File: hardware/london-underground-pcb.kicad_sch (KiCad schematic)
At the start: 335 parts

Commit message: first 150 LEDS placed
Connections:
- net LED10 is gone; now on net ROW10: LED91.4 (DI)
- net LED11 is gone; now on net ROW11: LED101.4 (DI)
- net LED12 is gone; now on net ROW12: LED111.4 (DI)
- net LED13 is gone; now on net ROW13: LED121.4 (DI)
- net LED14 is gone; now on net ROW14: LED131.4 (DI)
- net LED15 is gone; now on net ROW15: LED141.4 (DI)
- net LED16 is gone; now on net ROW16: LED151.4 (DI)
- net LED17 is gone; now on net ROW17: LED161.4 (DI)
- net LED18 is gone; now on net ROW18: LED171.4 (DI)
- net LED19 is gone; now on net ROW19: LED181.4 (DI)
- net LED2 is gone; now on net ROW2: LED11.4 (DI)
- net LED20 is gone; now on net ROW20: LED191.4 (DI)
- net LED21 is gone; now on net ROW21: LED201.4 (DI)
- net LED22 is gone; now on net ROW22: LED211.4 (DI)
- net LED23 is gone; now on net ROW23: LED221.4 (DI)
- net LED24 is gone; now on net ROW24: LED231.4 (DI)
- net LED25 is gone; now on net ROW25: LED241.4 (DI)
- net LED26 is gone; now on net ROW26: LED251.4 (DI)
- net LED27 is gone; now on net ROW27: LED261.4 (DI)
- net LED28 is gone; now on net ROW28: LED271.4 (DI)
- net LED29 is gone; now on net ROW29: LED281.4 (DI)
- net LED3 is gone; now on net ROW3: LED21.4 (DI)
- net LED30 is gone; now on net ROW30: LED291.4 (DI)
- net LED4 is gone; now on net ROW4: LED31.4 (DI)
- net LED5 is gone; now on net ROW5: LED41.4 (DI)
- net LED6 is gone; now on net ROW6: LED51.4 (DI)
- net LED7 is gone; now on net ROW7: LED61.4 (DI)
- net LED8 is gone; now on net ROW8: LED71.4 (DI)
- net LED9 is gone; now on net ROW9: LED81.4 (DI)

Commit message: Placed 570 LEDS,
Still need to do the routing
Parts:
- added LED301, LED302, LED303, LED304, LED305, LED306, LED307, LED308, LED309, LED310, LED311, LED312, LED313, LED314, LED315, LED316, LED317, LED318, LED319, LED320, LED321, LED322, LED323, LED324, LED325, LED326, LED327, LED328, LED329, LED330, LED331, LED332, LED333, LED334, LED335, LED336, LED337, LED338, LED339, LED340, LED341, LED342, LED343, LED344, LED345, LED346, LED347, LED348, LED349, LED350, LED351, LED352, LED353, LED354, LED355, LED356, LED357, LED358, LED359, LED360, LED361, LED362, LED363, LED364, LED365, LED366, LED367, LED368, LED369, LED370, LED371, LED372, LED373, LED374, LED375, LED376, LED377, LED378, LED379, LED380, LED381, LED382, LED383, LED384, LED385, LED386, LED387, LED388, LED389, LED390, LED391, LED392, LED393, LED394, LED395, LED396, LED397, LED398, LED399, LED400, LED401, LED402, LED403, LED404, LED405, LED406, LED407, LED408, LED409, LED410, LED411, LED412, LED413, LED414, LED415, LED416, LED417, LED418, LED419, LED420, LED421, LED422, LED423, LED424, LED425, LED426, LED427, LED428, LED429, LED430, LED431, LED432, LED433, LED434, LED435, LED436, LED437, LED438, LED439, LED440, LED441, LED442, LED443, LED444, LED445, LED446, LED447, LED448, LED449, LED450, LED451, LED452, LED453, LED454, LED455, LED456, LED457, LED458, LED459, LED460, LED461, LED462, LED463, LED464, LED465, LED466, LED467, LED468, LED469, LED470, LED471, LED472, LED473, LED474, LED475, LED476, LED477, LED478, LED479, LED480, LED481, LED482, LED483, LED484, LED485, LED486, LED487, LED488, LED489, LED490, LED491, LED492, LED493, LED494, LED495, LED496, LED497, LED498, LED499, LED500, LED501, LED502, LED503, LED504, LED505, LED506, LED507, LED508, LED509, LED510, LED511, LED512, LED513, LED514, LED515, LED516, LED517, LED518, LED519, LED520, LED521, LED522, LED523, LED524, LED525, LED526, LED527, LED528, LED529, LED530, LED531, LED532, LED533, LED534, LED535, LED536, LED537, LED538, LED539, LED540, LED541, LED542, LED543, LED544, LED545, LED546, LED547, LED548, LED549, LED550, LED551, LED552, LED553, LED554, LED555, LED556, LED557, LED558, LED559, LED560, LED561, LED562, LED563, LED564, LED565, LED566, LED567, LED568, LED569, LED570: XL-1615RGBC-WS2812B, XL-1615RGBC-WS2812B:LED-SMD_4P-L1.6-W1.5_XL-1615RGBC-WS2812B, symbol XL-1615RGBC-WS2812B:XL-1615RGBC-WS2812B
- added ROW31, ROW32, ROW33, ROW34, ROW35, ROW36, ROW37, ROW38, ROW39, ROW40, ROW41, ROW42, ROW43, ROW44, ROW45, ROW46, ROW47, ROW48, ROW49, ROW50: 10uF,10V,X5R, Capacitor_SMD:C_0402_1005Metric, symbol __sws_jlpcb:jlcpcb-1uF,25V,X5R
- renumbered ROW8 to ROW1, ROW6 to ROW10, ROW7 to ROW11, ROW9 to ROW2, ROW10 to ROW3, ROW11 to ROW4, ROW1 to ROW5, ROW2 to ROW6, ROW3 to ROW7, ROW4 to ROW8, ROW5 to ROW9
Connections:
- net +5V: now also LED301.2 (VDD), LED302.2 (VDD), LED303.2 (VDD), LED304.2 (VDD), LED305.2 (VDD), LED306.2 (VDD), LED307.2 (VDD), LED308.2 (VDD), LED309.2 (VDD), LED310.2 (VDD), LED311.2 (VDD), LED312.2 (VDD)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
- net GND: now also LED301.3 (GND), LED302.3 (GND), LED303.3 (GND), LED304.3 (GND), LED305.3 (GND), LED306.3 (GND), LED307.3 (GND), LED308.3 (GND), LED309.3 (GND), LED310.3 (GND), LED311.3 (GND), LED312.3 (GND)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
- net ROW31: now also LED301.4 (DI)
- new net: LED449.1 (DO), LED450.4 (DI)
- new net: LED332.1 (DO), LED333.4 (DI)
- new net: LED331.1 (DO), LED332.4 (DI)
- new net: LED303.1 (DO), LED304.4 (DI)
- new net: LED302.1 (DO), LED303.4 (DI)
- new net: LED398.1 (DO), LED399.4 (DI)
- new net: LED397.1 (DO), LED398.4 (DI)
- new net: LED393.1 (DO), LED394.4 (DI)
- new net: LED392.1 (DO), LED393.4 (DI)
- new net: LED325.1 (DO), LED326.4 (DI)
- new net: LED324.1 (DO), LED325.4 (DI)
- new net: LED519.1 (DO), LED520.4 (DI)
- new net: LED518.1 (DO), LED519.4 (DI)
- new net: LED421.1 (DO), LED422.4 (DI)
- new net: LED356.1 (DO), LED357.4 (DI)
- new net: LED355.1 (DO), LED356.4 (DI)
- new net: LED373.1 (DO), LED374.4 (DI)
- new net: LED372.1 (DO), LED373.4 (DI)
- new net: LED308.1 (DO), LED309.4 (DI)
- new net: LED307.1 (DO), LED308.4 (DI)
- new net: LED384.1 (DO), LED385.4 (DI)
- new net: LED383.1 (DO), LED384.4 (DI)
- new net: LED462.1 (DO), LED463.4 (DI)
- new net: LED461.1 (DO), LED462.4 (DI)
- new net: LED552.1 (DO), LED553.4 (DI)
- new net: LED551.1 (DO), LED552.4 (DI)
- new net: LED469.1 (DO), LED470.4 (DI)
- new net: LED468.1 (DO), LED469.4 (DI)
- new net: LED549.1 (DO), LED550.4 (DI)
- new net: LED408.1 (DO), LED409.4 (DI)
- new net: LED407.1 (DO), LED408.4 (DI)
- new net: LED347.1 (DO), LED348.4 (DI)
- new net: LED346.1 (DO), LED347.4 (DI)
- new net: LED387.1 (DO), LED388.4 (DI)
- new net: LED386.1 (DO), LED387.4 (DI)
- new net: LED555.1 (DO), LED556.4 (DI)
- new net: LED554.1 (DO), LED555.4 (DI)
- new net: LED457.1 (DO), LED458.4 (DI)
- new net: LED456.1 (DO), LED457.4 (DI)
- new net: LED569.1 (DO), LED570.4 (DI)
- new net: LED568.1 (DO), LED569.4 (DI)
- new net: LED463.1 (DO), LED464.4 (DI)
- new net: LED453.1 (DO), LED454.4 (DI)
- new net: LED452.1 (DO), LED453.4 (DI)
- new net: LED399.1 (DO), LED400.4 (DI)
- new net: LED496.1 (DO), LED497.4 (DI)
- new net: LED495.1 (DO), LED496.4 (DI)
- new net: LED417.1 (DO), LED418.4 (DI)
- new net: LED416.1 (DO), LED417.4 (DI)
- new net: LED503.1 (DO), LED504.4 (DI)
- new net: LED502.1 (DO), LED503.4 (DI)
- new net: LED445.1 (DO), LED446.4 (DI)
- new net: LED444.1 (DO), LED445.4 (DI)
- new net: LED349.1 (DO), LED350.4 (DI)
- new net: LED406.1 (DO), LED407.4 (DI)
- new net: LED557.1 (DO), LED558.4 (DI)
- new net: LED556.1 (DO), LED557.4 (DI)
- new net: LED363.1 (DO), LED364.4 (DI)
- new net: LED362.1 (DO), LED363.4 (DI)
- new net: LED364.1 (DO), LED365.4 (DI)
- new net: LED446.1 (DO), LED447.4 (DI)
- new net: LED394.1 (DO), LED395.4 (DI)
- new net: LED467.1 (DO), LED468.4 (DI)
- new net: LED544.1 (DO), LED545.4 (DI)
- new net: LED543.1 (DO), LED544.4 (DI)
- new net: LED409.1 (DO), LED410.4 (DI)
- new net: LED525.1 (DO), LED526.4 (DI)
- new net: LED524.1 (DO), LED525.4 (DI)
- new net: LED517.1 (DO), LED518.4 (DI)
- new net: LED516.1 (DO), LED517.4 (DI)
- new net: LED301.1 (DO), LED302.4 (DI)
- new net: LED548.1 (DO), LED549.4 (DI)
- new net: LED547.1 (DO), LED548.4 (DI)
- new net: LED427.1 (DO), LED428.4 (DI)
- new net: LED426.1 (DO), LED427.4 (DI)
- new net: LED439.1 (DO), LED440.4 (DI)
- new net: LED477.1 (DO), LED478.4 (DI)
- new net: LED476.1 (DO), LED477.4 (DI)
- new net: LED546.1 (DO), LED547.4 (DI)
- new net: LED478.1 (DO), LED479.4 (DI)
- new net: LED371.1 (DO), LED372.4 (DI)
- new net: LED377.1 (DO), LED378.4 (DI)
- new net: LED376.1 (DO), LED377.4 (DI)
- new net: LED526.1 (DO), LED527.4 (DI)
- new net: LED388.1 (DO), LED389.4 (DI)
- new net: LED403.1 (DO), LED404.4 (DI)
- new net: LED402.1 (DO), LED403.4 (DI)
- new net: LED396.1 (DO), LED397.4 (DI)
- new net: LED395.1 (DO), LED396.4 (DI)
- new net: LED466.1 (DO), LED467.4 (DI)
- new net: LED499.1 (DO), LED500.4 (DI)
- new net: LED389.1 (DO), LED390.4 (DI)
- new net: LED375.1 (DO), LED376.4 (DI)
- new net: LED374.1 (DO), LED375.4 (DI)
- new net: LED405.1 (DO), LED406.4 (DI)
- new net: LED404.1 (DO), LED405.4 (DI)
- new net: LED424.1 (DO), LED425.4 (DI)
- new net: LED423.1 (DO), LED424.4 (DI)
- new net: LED504.1 (DO), LED505.4 (DI)
- new net: LED326.1 (DO), LED327.4 (DI)
- new net: LED425.1 (DO), LED426.4 (DI)
- new net: LED443.1 (DO), LED444.4 (DI)
- new net: LED442.1 (DO), LED443.4 (DI)
- new net: LED348.1 (DO), LED349.4 (DI)
- new net: LED521.1 (DO), LED522.4 (DI)
- new net: LED489.1 (DO), LED490.4 (DI)
- new net: LED336.1 (DO), LED337.4 (DI)
- new net: LED335.1 (DO), LED336.4 (DI)
- new net: LED508.1 (DO), LED509.4 (DI)
- new net: LED507.1 (DO), LED508.4 (DI)
- new net: LED559.1 (DO), LED560.4 (DI)
- new net: LED558.1 (DO), LED559.4 (DI)
- new net: LED309.1 (DO), LED310.4 (DI)
- new net: LED401.1 (DO), LED402.4 (DI)
- new net: LED431.1 (DO), LED432.4 (DI)
- new net: LED537.1 (DO), LED538.4 (DI)
- new net: LED536.1 (DO), LED537.4 (DI)
- new net: LED438.1 (DO), LED439.4 (DI)
- new net: LED509.1 (DO), LED510.4 (DI)
- new net: LED483.1 (DO), LED484.4 (DI)
- new net: LED482.1 (DO), LED483.4 (DI)
- new net: LED418.1 (DO), LED419.4 (DI)
- new net: LED474.1 (DO), LED475.4 (DI)
- new net: LED473.1 (DO), LED474.4 (DI)
- new net: LED542.1 (DO), LED543.4 (DI)
- new net: LED523.1 (DO), LED524.4 (DI)
- new net: LED541.1 (DO), LED542.4 (DI)
- new net: LED337.1 (DO), LED338.4 (DI)
- new net: LED369.1 (DO), LED370.4 (DI)
- new net: LED485.1 (DO), LED486.4 (DI)
- new net: LED484.1 (DO), LED485.4 (DI)
- new net: LED333.1 (DO), LED334.4 (DI)
- new net: LED501.1 (DO), LED502.4 (DI)
- new net: LED471.1 (DO), LED472.4 (DI)
- new net: LED447.1 (DO), LED448.4 (DI)
- new net: LED327.1 (DO), LED328.4 (DI)
- new net: LED328.1 (DO), LED329.4 (DI)
- new net: LED354.1 (DO), LED355.4 (DI)
- new net: LED481.1 (DO), LED482.4 (DI)
- new net: LED451.1 (DO), LED452.4 (DI)
- new net: LED306.1 (DO), LED307.4 (DI)
- new net: LED562.1 (DO), LED563.4 (DI)
- new net: LED561.1 (DO), LED562.4 (DI)
- new net: LED535.1 (DO), LED536.4 (DI)
- new net: LED534.1 (DO), LED535.4 (DI)
- new net: LED339.1 (DO), LED340.4 (DI)
- new net: LED455.1 (DO), LED456.4 (DI)
- new net: LED382.1 (DO), LED383.4 (DI)
- new net: LED357.1 (DO), LED358.4 (DI)
- new net: LED323.1 (DO), LED324.4 (DI)
- new net: LED322.1 (DO), LED323.4 (DI)
- new net: LED412.1 (DO), LED413.4 (DI)
- new net: LED411.1 (DO), LED412.4 (DI)
- new net: LED531.1 (DO), LED532.4 (DI)
- new net: LED316.1 (DO), LED317.4 (DI)
- new net: LED315.1 (DO), LED316.4 (DI)
- new net: LED368.1 (DO), LED369.4 (DI)
- new net: LED367.1 (DO), LED368.4 (DI)
- new net: LED498.1 (DO), LED499.4 (DI)
- new net: LED497.1 (DO), LED498.4 (DI)
- new net: LED472.1 (DO), LED473.4 (DI)
- new net: LED312.1 (DO), LED313.4 (DI)
- new net: LED311.1 (DO), LED312.4 (DI)
- new net: LED545.1 (DO), LED546.4 (DI)
- new net: LED415.1 (DO), LED416.4 (DI)
- new net: LED459.1 (DO), LED460.4 (DI)
- new net: LED361.1 (DO), LED362.4 (DI)
- new net: LED353.1 (DO), LED354.4 (DI)
- new net: LED352.1 (DO), LED353.4 (DI)
- new net: LED553.1 (DO), LED554.4 (DI)
- new net: LED567.1 (DO), LED568.4 (DI)
- new net: LED479.1 (DO), LED480.4 (DI)
- new net: LED565.1 (DO), LED566.4 (DI)
- new net: LED564.1 (DO), LED565.4 (DI)
- new net: LED491.1 (DO), LED492.4 (DI)
- new net: LED422.1 (DO), LED423.4 (DI)
- new net: LED345.1 (DO), LED346.4 (DI)
- new net: LED488.1 (DO), LED489.4 (DI)
- new net: LED487.1 (DO), LED488.4 (DI)
- new net: LED511.1 (DO), LED512.4 (DI)
- new net: LED566.1 (DO), LED567.4 (DI)
- new net: LED419.1 (DO), LED420.4 (DI)
- new net: LED515.1 (DO), LED516.4 (DI)
- new net: LED448.1 (DO), LED449.4 (DI)
- new net: LED437.1 (DO), LED438.4 (DI)
- new net: LED436.1 (DO), LED437.4 (DI)
- new net: LED358.1 (DO), LED359.4 (DI)
- new net: LED314.1 (DO), LED315.4 (DI)
- new net: LED313.1 (DO), LED314.4 (DI)
- new net: LED506.1 (DO), LED507.4 (DI)
- new net: LED338.1 (DO), LED339.4 (DI)
- new net: LED414.1 (DO), LED415.4 (DI)
- new net: LED413.1 (DO), LED414.4 (DI)
- new net: LED527.1 (DO), LED528.4 (DI)
- new net: LED514.1 (DO), LED515.4 (DI)
- new net: LED513.1 (DO), LED514.4 (DI)
- new net: LED528.1 (DO), LED529.4 (DI)
- new net: LED305.1 (DO), LED306.4 (DI)
- new net: LED429.1 (DO), LED430.4 (DI)
- new net: LED428.1 (DO), LED429.4 (DI)
- new net: LED365.1 (DO), LED366.4 (DI)
- new net: LED454.1 (DO), LED455.4 (DI)
- new net: LED458.1 (DO), LED459.4 (DI)
- new net: LED344.1 (DO), LED345.4 (DI)
- new net: LED533.1 (DO), LED534.4 (DI)
- new net: LED512.1 (DO), LED513.4 (DI)
- new net: LED391.1 (DO), LED392.4 (DI)
- new net: LED359.1 (DO), LED360.4 (DI)
- new net: LED493.1 (DO), LED494.4 (DI)
- new net: LED492.1 (DO), LED493.4 (DI)
- new net: LED317.1 (DO), LED318.4 (DI)
- new net: LED475.1 (DO), LED476.4 (DI)
- new net: LED538.1 (DO), LED539.4 (DI)
- new net: LED464.1 (DO), LED465.4 (DI)
- new net: LED385.1 (DO), LED386.4 (DI)
- new net: LED343.1 (DO), LED344.4 (DI)
- new net: LED494.1 (DO), LED495.4 (DI)
- new net: LED366.1 (DO), LED367.4 (DI)
- new net: LED486.1 (DO), LED487.4 (DI)
- new net: LED318.1 (DO), LED319.4 (DI)
- new net: LED532.1 (DO), LED533.4 (DI)
- new net: LED539.1 (DO), LED540.4 (DI)
- new net: LED529.1 (DO), LED530.4 (DI)
- new net: LED465.1 (DO), LED466.4 (DI)
- new net: LED505.1 (DO), LED506.4 (DI)
- new net: LED381.1 (DO), LED382.4 (DI)
- new net: LED378.1 (DO), LED379.4 (DI)
- new net: LED342.1 (DO), LED343.4 (DI)
- new net: LED334.1 (DO), LED335.4 (DI)
- new net: LED379.1 (DO), LED380.4 (DI)
- new net: LED563.1 (DO), LED564.4 (DI)
- new net: LED351.1 (DO), LED352.4 (DI)
- new net: LED441.1 (DO), LED442.4 (DI)
- new net: LED329.1 (DO), LED330.4 (DI)
- new net: LED433.1 (DO), LED434.4 (DI)
- new net: LED432.1 (DO), LED433.4 (DI)
- new net: LED434.1 (DO), LED435.4 (DI)
- new net: LED435.1 (DO), LED436.4 (DI)
- new net: LED522.1 (DO), LED523.4 (DI)
- new net: LED304.1 (DO), LED305.4 (DI)
- new net: LED321.1 (DO), LED322.4 (DI)
- new net: LED341.1 (DO), LED342.4 (DI)
- new net: LED319.1 (DO), LED320.4 (DI)
- new net ROW32: LED310.1 (DO), LED311.4 (DI)
- new net ROW33: LED320.1 (DO), LED321.4 (DI)
- new net ROW34: LED330.1 (DO), LED331.4 (DI)
- new net ROW35: LED340.1 (DO), LED341.4 (DI)
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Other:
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
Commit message: Resolving DRC
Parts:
- added ROW51, ROW52, ROW53, ROW54, ROW55, ROW56, ROW57, ROW58: 10uF,10V,X5R, Capacitor_SMD:C_0402_1005Metric, symbol __sws_jlpcb:jlcpcb-1uF,25V,X5R
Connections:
- net +5V: now also ROW51.2, ROW52.2, ROW53.2, ROW54.2, ROW55.2, ROW56.2, ROW57.2, ROW58.2
- net GND: now also ROW51.1, ROW52.1, ROW53.1, ROW54.1, ROW55.1, ROW56.1, ROW57.1, ROW58.1
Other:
- moved on the sheet: ROW1, ROW10, ROW11, ROW12, ROW13, ROW14, ROW15, ROW16, ROW17, ROW18, ROW19, ROW2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

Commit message: Updated parts list from JLCPCB
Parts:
- removed J1: ~, SWS-Library:XIAO, symbol XIAO:XIAO
- removed LED570: XL-1615RGBC-WS2812B, XL-1615RGBC-WS2812B:LED-SMD_4P-L1.6-W1.5_XL-1615RGBC-WS2812B, symbol XL-1615RGBC-WS2812B:XL-1615RGBC-WS2812B
- added +5V1, +5V2, +5V3, +5V4, +5V5, +5V6, +5V7, LED_IN1, LED_OUT1: TestPoint, TestPoint:TestPoint_Pad_3.0x3.0mm, symbol Connector:TestPoint
- added SW1, SW2, SW3, SW4: TS-1187A-B-A-B, JLCPCB-C318884:SW-SMD_4P-L5.1-W5.1-P3.70-LS6.5-TL_H1.5, symbol JLCPCB-C318884:TS-1187A-B-A-B
- added U1: XIAO-RP2040-DIP, Seeed Studio XIAO:XIAO-SAMD21-SMD, symbol Seeed Studio XIAO:XIAO-RP2040-DIP
- LED1, LED10, LED100, LED101, LED102, LED103, LED104, LED105, LED106, LED107, LED108, LED109, LED11, LED110, LED111, LED112, LED113, LED114, LED115, LED116, LED117, LED118, LED119, LED12, LED120, LED121, LED122, LED123, LED124, LED125, LED126, LED127, LED128, LED129, LED13, LED130, LED131, LED132, LED133, LED134, LED135, LED136, LED137, LED138, LED139, LED14, LED140, LED141, LED142, LED143, LED144, LED145, LED146, LED147, LED148, LED149, LED15, LED150, LED151, LED152, LED153, LED154, LED155, LED156, LED157, LED158, LED159, LED16, LED160, LED161, LED162, LED163, LED164, LED165, LED166, LED167, LED168, LED169, LED17, LED170, LED171, LED172, LED173, LED174, LED175, LED176, LED177, LED178, LED179, LED18, LED180, LED181, LED182, LED183, LED184, LED185, LED186, LED187, LED188, LED189, LED19, LED190, LED191, LED192, LED193, LED194, LED195, LED196, LED197, LED198, LED199, LED2, LED20, LED200, LED201, LED202, LED203, LED204, LED205, LED206, LED207, LED208, LED209, LED21, LED210, LED211, LED212, LED213, LED214, LED215, LED216, LED217, LED218, LED219, LED22, LED220, LED221, LED222, LED223, LED224, LED225, LED226, LED227, LED228, LED229, LED23, LED230, LED231, LED232, LED233, LED234, LED235, LED236, LED237, LED238, LED239, LED24, LED240, LED241, LED242, LED243, LED244, LED245, LED246, LED247, LED248, LED249, LED25, LED250, LED251, LED252, LED253, LED254, LED255, LED256, LED257, LED258, LED259, LED26, LED260, LED261, LED262, LED263, LED264, LED265, LED266, LED267, LED268, LED269, LED27, LED270, LED271, LED272, LED273, LED274, LED275, LED276, LED277, LED278, LED279, LED28, LED280, LED281, LED282, LED283, LED284, LED285, LED286, LED287, LED288, LED289, LED29, LED290, LED291, LED292, LED293, LED294, LED295, LED296, LED297, LED298, LED299, LED3, LED30, LED300, LED301, LED302, LED303, LED304, LED305, LED306, LED307, LED308, LED309, LED31, LED310, LED311, LED312, LED313, LED314, LED315, LED316, LED317, LED318, LED319, LED32, LED320, LED321, LED322, LED323, LED324, LED325, LED326, LED327, LED328, LED329, LED33, LED330, LED331, LED332, LED333, LED334, LED335, LED336, LED337, LED338, LED339, LED34, LED340, LED341, LED342, LED343, LED344, LED345, LED346, LED347, LED348, LED349, LED35, LED350, LED351, LED352, LED353, LED354, LED355, LED356, LED357, LED358, LED359, LED36, LED360, LED361, LED362, LED363, LED364, LED365, LED366, LED367, LED368, LED369, LED37, LED370, LED371, LED372, LED373, LED374, LED375, LED376, LED377, LED378, LED379, LED38, LED380, LED381, LED382, LED383, LED384, LED385, LED386, LED387, LED388, LED389, LED39, LED390, LED391, LED392, LED393, LED394, LED395, LED396, LED397, LED398, LED399, LED4, LED40, LED400, LED401, LED402, LED403, LED404, LED405, LED406, LED407, LED408, LED409, LED41, LED410, LED411, LED412, LED413, LED414, LED415, LED416, LED417, LED418, LED419, LED42, LED420, LED421, LED422, LED423, LED424, LED425, LED426, LED427, LED428, LED429, LED43, LED430, LED431, LED432, LED433, LED434, LED435, LED436, LED437, LED438, LED439, LED44, LED440, LED441, LED442, LED443, LED444, LED445, LED446, LED447, LED448, LED449, LED45, LED450, LED451, LED452, LED453, LED454, LED455, LED456, LED457, LED458, LED459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: footprint XL-1615RGBC-WS2812B:LED-SMD_4P-L1.6-W1.5_XL-1615RGBC-WS2812B -> JLCPCB-C5349954:LED-SMD_4P-L1.6-W1.5_XL-1615RGBC-WS2812B
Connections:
- net +5V: now also +5V1.1, +5V2.1, +5V3.1, +5V4.1, +5V5.1, +5V6.1, +5V7.1, U1.14 (VBUS)
- net GND: now also SW1.3 (C), SW1.4 (D), SW2.3 (C), SW2.4 (D), SW3.3 (C), SW3.4 (D), SW4.3 (C), SW4.4 (D), U1.13 (GND)
- net LED_IN: now also LED_IN1.1, U1.8 (GPIO1/RX)
- net ROW58: now also LED569.1 (DO), LED_OUT1.1
- new net BUTTON_01: SW1.1 (A), U1.1 (GPIO26/ADC0/A0)
- new net BUTTON_02: SW2.1 (A), U1.2 (GPIO27/ADC1/A1)
- new net BUTTON_03: SW3.2 (B), U1.3 (GPIO28/ADC2/A2)
- new net BUTTON_04: SW4.2 (B), U1.4 (GPIO29/ADC3/A3)
- no-connect marks 15 -> 11
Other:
- moved on the sheet: LED101, LED102, LED103, LED104, LED105, LED106, LED107, LED108, LED109, LED110, LED111, LED112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

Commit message: 2025-nov-25 - cleanup ready for review
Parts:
- removed LED101, LED102, LED103, LED104, LED105, LED106, LED107, LED108, LED109, LED110, LED111, LED112, LED113, LED114, LED115, LED116, LED117, LED118, LED119, LED120, LED121, LED122, LED123, LED124, LED125, LED126, LED127, LED128, LED129, LED130, LED131, LED132, LED133, LED134, LED135, LED136, LED137, LED138, LED139, LED140, LED141, LED142, LED143, LED144, LED145, LED146, LED147, LED148, LED149, LED150, LED151, LED152, LED153, LED154, LED155, LED156, LED157, LED158, LED159, LED160, LED161, LED162, LED163, LED164, LED165, LED166, LED167, LED168, LED169, LED170, LED171, LED172, LED173, LED174, LED175, LED176, LED177, LED178, LED179, LED180, LED181, LED182, LED183, LED184, LED185, LED186, LED187, LED188, LED189, LED190, LED191, LED192, LED193, LED194, LED195, LED196, LED197, LED198, LED199, LED200, LED201, LED202, LED203, LED204, LED205, LED206, LED207, LED208, LED209, LED210, LED211, LED212, LED213, LED214, LED215, LED216, LED217, LED218, LED219, LED220, LED221, LED222, LED223, LED224, LED225, LED226, LED227, LED228, LED229, LED230, LED231, LED232, LED233, LED234, LED235, LED236, LED237, LED238, LED239, LED240, LED241, LED242, LED243, LED244, LED245, LED246, LED247, LED248, LED249, LED250, LED251, LED252, LED253, LED254, LED255, LED256, LED257, LED258, LED259, LED260, LED261, LED262, LED263, LED264, LED265, LED266, LED267, LED268, LED269, LED270, LED271, LED272, LED273, LED274, LED275, LED276, LED277, LED278, LED279, LED280, LED281, LED282, LED283, LED284, LED285, LED286, LED287, LED288, LED289, LED290, LED291, LED292, LED293, LED294, LED295, LED296, LED297, LED298, LED299, LED300, LED301, LED302, LED303, LED304, LED305, LED306, LED307, LED308, LED309, LED310, LED311, LED312, LED313, LED314, LED315, LED316, LED317, LED318, LED319, LED320, LED321, LED322, LED323, LED324, LED325, LED326, LED327, LED328, LED329, LED330, LED331, LED332, LED333, LED334, LED335, LED336, LED337, LED338, LED339, LED340, LED341, LED342, LED343, LED344, LED345, LED346, LED347, LED348, LED349, LED350, LED351, LED352, LED353, LED354, LED355, LED356, LED357, LED358, LED359, LED360, LED361, LED362, LED363, LED364, LED365, LED366, LED367, LED368, LED369, LED370, LED371, LED372, LED373, LED374, LED375, LED376, LED377, LED378, LED379, LED380, LED381, LED382, LED383, LED384, LED385, LED386, LED387, LED388, LED389, LED390, LED391, LED392, LED393, LED394, LED395, LED396, LED397, LED398, LED399, LED400, LED401, LED402, LED403, LED404, LED405, LED406, LED407, LED408, LED409, LED410, LED411, LED412, LED413, LED414, LED415, LED416, LED417, LED418, LED419, LED420, LED421, LED422, LED423, LED424, LED425, LED426, LED427, LED428, LED429, LED430, LED431, LED432, LED433, LED434, LED435, LED436, LED437, LED438, LED439, LED440, LED441, LED442, LED443, LED444, LED445, LED446, LED447, LED448, LED449, LED450, LED451, LED452, LED453, LED454, LED455, LED456, LED457, LED458, LED459, LED460, LED461, LED462, LED463, LED464, LED465, LED466, LED467, LED468, LED469, LED470, LED471, LED472, LED473, LED474, LED475, LED476, LED477, LED478, LED479, LED480, LED481, LED482, LED483, LED484, LED485, LED486, LED487, LED488, LED489, LED490, LED491, LED492, LED493, LED494, LED495, LED496, LED497, LED498, LED499, LED500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: XL-1615RGBC-WS2812B, JLCPCB-C5349954:LED-SMD_4P-L1.6-W1.5_XL-1615RGBC-WS2812B, symbol XL-1615RGBC-WS2812B:XL-1615RGBC-WS2812B
- added +5V8, GND1: TestPoint, TestPoint:TestPoint_Pad_3.0x3.0mm, symbol Connector:TestPoint
- added LED101, LED102, LED103, LED104, LED105, LED106, LED107, LED108, LED109, LED110, LED111, LED112, LED113, LED114, LED115, LED116, LED117, LED118, LED119, LED120, LED121, LED122, LED123, LED124, LED125, LED126, LED127, LED128, LED129, LED130, LED131, LED132, LED133, LED134, LED135, LED136, LED137, LED138, LED139, LED140, LED141, LED142, LED143, LED144, LED145, LED146, LED147, LED148, LED149, LED150, LED151, LED152, LED153, LED154, LED155, LED156, LED157, LED158, LED159, LED160, LED161, LED162, LED163, LED164, LED165, LED166, LED167, LED168, LED169, LED170, LED171, LED172, LED173, LED174, LED175, LED176, LED177, LED178, LED179, LED180, LED181, LED182, LED183, LED184, LED185, LED186, LED187, LED188, LED189, LED190, LED191, LED192, LED193, LED194, LED195, LED196, LED197, LED198, LED199, LED200, LED201, LED202, LED203, LED204, LED205, LED206, LED207, LED208, LED209, LED210, LED211, LED212, LED213, LED214, LED215, LED216, LED217, LED218, LED219, LED220, LED221, LED222, LED223, LED224, LED225, LED226, LED227, LED228, LED229, LED230, LED231, LED232, LED233, LED234, LED235, LED236, LED237, LED238, LED239, LED240, LED241, LED242, LED243, LED244, LED245, LED246, LED247, LED248, LED249, LED250, LED251, LED252, LED253, LED254, LED255, LED256, LED257, LED258, LED259, LED260, LED261, LED262, LED263, LED264, LED265, LED266, LED267, LED268, LED269, LED270, LED271, LED272, LED273, LED274, LED275, LED276, LED277, LED278, LED279, LED280, LED281, LED282, LED283, LED284, LED285, LED286, LED287, LED288, LED289, LED290, LED291, LED292, LED293, LED294, LED295, LED296, LED297, LED298, LED299, LED300, LED301, LED302, LED303, LED304, LED305, LED306, LED307, LED308, LED309, LED310, LED311, LED312, LED313, LED314, LED315, LED316, LED317, LED318, LED319, LED320, LED321, LED322, LED323, LED324, LED325, LED326, LED327, LED328, LED329, LED330, LED331, LED332, LED333, LED334, LED335, LED336, LED337, LED338, LED339, LED340, LED341, LED342, LED343, LED344, LED345, LED346, LED347, LED348, LED349, LED350, LED351, LED352, LED353, LED354, LED355, LED356, LED357, LED358, LED359, LED360, LED361, LED362, LED363, LED364, LED365, LED366, LED367, LED368, LED369, LED370, LED371, LED372, LED373, LED374, LED375, LED376, LED377, LED378, LED379, LED380, LED381, LED382, LED383, LED384, LED385, LED386, LED387, LED388, LED389, LED390, LED391, LED392, LED393, LED394, LED395, LED396, LED397, LED398, LED399, LED400, LED401, LED402, LED403, LED404, LED405, LED406, LED407, LED408, LED409, LED410, LED411, LED412, LED413, LED414, LED415, LED416, LED417, LED418, LED419, LED420, LED421, LED422, LED423, LED424, LED425, LED426, LED427, LED428, LED429, LED430, LED431, LED432, LED433, LED434, LED435, LED436, LED437, LED438, LED439, LED440, LED441, LED442, LED443, LED444, LED445, LED446, LED447, LED448, LED449, LED450, LED451, LED452, LED453, LED454, LED455, LED456, LED457, LED458, LED459, LED460, LED461, LED462, LED463, LED464, LED465, LED466, LED467, LED468, LED469, LED470, LED471, LED472, LED473, LED474, LED475, LED476, LED477, LED478, LED479, LED480, LED481, LED482, LED483, LED484, LED485, LED486, LED487, LED488, LED489, LED490, LED491, LED492, LED493, LED494, LED495, LED496, LED497, LED498, LED499, LED500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: XL-1615RGBC-WS2812B, JLCPCB-C5349954:LED-SMD_4P-L1.6-W1.5_XL-1615RGBC-WS2812B-1, symbol JLCPCB-C5349954:XL-1615RGBC-WS2812B
- added R1, R2, R3, R4, R5, R6: 1206W4F0000T5E, Resistor_SMD:R_1206_3216Metric, symbol JLCPCB-C17888:1206W4F0000T5E
- added ROW59, ROW60: 10uF,10V,X5R, Capacitor_SMD:C_0402_1005Metric, symbol __sws_jlpcb:jlcpcb-1uF,25V,X5R
- H1, H2, H3, H4: footprint MountingHole:MountingHole_3.2mm_M3 -> MountingHole:MountingHole_3.2mm_M3_DIN965_Pad
- LED1, LED10, LED100, LED11, LED12, LED13, LED14, LED15, LED16, LED17, LED18, LED19, LED2, LED20, LED21, LED22, LED23, LED24, LED25, LED26, LED27, LED28, LED29, LED3, LED30, LED31, LED32, LED33, LED34, LED35, LED36, LED37, LED38, LED39, LED4, LED40, LED41, LED42, LED43, LED44, LED45, LED46, LED47, LED48, LED49, LED5, LED50, LED51, LED52, LED53, LED54, LED55, LED56, LED57, LED58, LED59, LED6, LED60, LED61, LED62, LED63, LED64, LED65, LED66, LED67, LED68, LED69, LED7, LED70, LED71, LED72, LED73, LED74, LED75, LED76, LED77, LED78, LED79, LED8, LED80, LED81, LED82, LED83, LED84, LED85, LED86, LED87, LED88, LED89, LED9, LED90, LED91, LED92, LED93, LED94, LED95, LED96, LED97, LED98, LED99: footprint JLCPCB-C5349954:LED-SMD_4P-L1.6-W1.5_XL-1615RGBC-WS2812B -> JLCPCB-C5349954:LED-SMD_4P-L1.6-W1.5_XL-1615RGBC-WS2812B-1; symbol XL-1615RGBC-WS2812B:XL-1615RGBC-WS2812B -> JLCPCB-C5349954:XL-1615RGBC-WS2812B
- SW1, SW4: now not fitted
- SW2: renamed from SW3; now not fitted
- SW3: renamed from SW2; now not fitted
- U1: footprint Seeed Studio XIAO:XIAO-SAMD21-SMD -> Seeed Studio XIAO:XIAO-RP2040-SMD
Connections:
- net +5V: now also LED1.3 (VDD), LED10.3 (VDD), LED100.3 (VDD), LED11.3 (VDD), LED12.3 (VDD), LED13.3 (VDD), LED14.3 (VDD), LED15.3 (VDD), LED16.3 (VDD), LED17.3 (VDD), LED18.3 (VDD), LED19.3 (VDD)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; no longer LED1.2 (VDD), LED10.2 (VDD), LED100.2 (VDD), LED11.2 (VDD), LED12.2 (VDD), LED13.2 (VDD), LED14.2 (VDD), LED15.2 (VDD), LED16.2 (VDD), LED17.2 (VDD), LED18.2 (VDD), LED19.2 (VDD)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
- net GND: now also LED1.1 (GND), LED10.1 (GND), LED100.1 (GND), LED11.1 (GND), LED12.1 (GND), LED13.1 (GND), LED14.1 (GND), LED15.1 (GND), LED16.1 (GND), LED17.1 (GND), LED18.1 (GND), LED19.1 (GND)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; no longer LED1.3 (GND), LED10.3 (GND), LED100.3 (GND), LED11.3 (GND), LED12.3 (GND), LED13.3 (GND), LED14.3 (GND), LED15.3 (GND), LED16.3 (GND), LED17.3 (GND), LED18.3 (GND), LED19.3 (GND)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
- net LED_IN: now also R2.1; no longer LED1.4 (DI)
- net ROW10: now also LED90.4 (DO), LED91.2 (DI); no longer LED90.1 (DO), LED91.4 (DI)
- net ROW11: now also LED101.2 (DI), R1.2; no longer LED100.1 (DO)
- net ROW12: now also LED110.4 (DO), LED111.2 (DI)
- net ROW13: now also LED120.4 (DO), LED121.2 (DI)
- net ROW14: now also LED130.4 (DO), LED131.2 (DI)
- net ROW15: now also LED140.4 (DO), LED141.2 (DI)
- net ROW16: now also LED150.4 (DO), LED151.2 (DI)
- net ROW17: now also LED160.4 (DO), LED161.2 (DI)
- net ROW18: now also LED170.4 (DO), LED171.2 (DI)
- net ROW19: now also LED180.4 (DO), LED181.2 (DI)
- net ROW2: now also LED10.4 (DO), LED11.2 (DI); no longer LED10.1 (DO), LED11.4 (DI)
- net ROW20: now also LED190.4 (DO), LED191.2 (DI)
- net ROW21: now also LED201.2 (DI), R3.2
- net ROW22: now also LED210.4 (DO), LED211.2 (DI)
- net ROW23: now also LED220.4 (DO), LED221.2 (DI)
- net ROW24: now also LED230.4 (DO), LED231.2 (DI)
- net ROW25: now also LED240.4 (DO), LED241.2 (DI)
- net ROW26: now also LED250.4 (DO), LED251.2 (DI)
- net ROW27: now also LED260.4 (DO), LED261.2 (DI)
- net ROW28: now also LED270.4 (DO), LED271.2 (DI)
- net ROW29: now also LED280.4 (DO), LED281.2 (DI)
- net ROW3: now also LED20.4 (DO), LED21.2 (DI); no longer LED20.1 (DO), LED21.4 (DI)
- net ROW30: now also LED290.4 (DO), LED291.2 (DI)
- net ROW31: now also LED301.2 (DI), R4.2
- net ROW32: now also LED310.4 (DO), LED311.2 (DI)
- net ROW33: now also LED320.4 (DO), LED321.2 (DI)
- net ROW34: now also LED330.4 (DO), LED331.2 (DI)
- net ROW35: now also LED340.4 (DO), LED341.2 (DI)
- net ROW36: now also LED350.4 (DO), LED351.2 (DI)
- net ROW37: now also LED360.4 (DO), LED361.2 (DI)
- net ROW38: now also LED370.4 (DO), LED371.2 (DI)
- net ROW39: now also LED380.4 (DO), LED381.2 (DI)
- net ROW4: now also LED30.4 (DO), LED31.2 (DI); no longer LED30.1 (DO), LED31.4 (DI)
- net ROW40: now also LED390.4 (DO), LED391.2 (DI)
- net ROW41: now also LED401.2 (DI), R5.2
- net ROW42: now also LED410.4 (DO), LED411.2 (DI)
- net ROW43: now also LED420.4 (DO), LED421.2 (DI)
- net ROW44: now also LED430.4 (DO), LED431.2 (DI)
- net ROW45: now also LED440.4 (DO), LED441.2 (DI)
- net ROW46: now also LED450.4 (DO), LED451.2 (DI)
- net ROW47: now also LED460.4 (DO), LED461.2 (DI)
- net ROW48: now also LED470.4 (DO), LED471.2 (DI)
- net ROW49: now also LED480.4 (DO), LED481.2 (DI)
- net ROW5: now also LED40.4 (DO), LED41.2 (DI); no longer LED40.1 (DO), LED41.4 (DI)
- net ROW50: now also LED490.4 (DO), LED491.2 (DI)
- net ROW51: now also LED501.2 (DI), R6.2
- net ROW52: now also LED510.4 (DO), LED511.2 (DI)
- net ROW53: now also LED520.4 (DO), LED521.2 (DI)
- net ROW54: now also LED530.4 (DO), LED531.2 (DI)
- net ROW55: now also LED540.4 (DO), LED541.2 (DI)
- net ROW56: now also LED550.4 (DO), LED551.2 (DI)
- net ROW57: now also LED560.4 (DO), LED561.2 (DI)
- net ROW6: now also LED50.4 (DO), LED51.2 (DI); no longer LED50.1 (DO), LED51.4 (DI)
- net ROW7: now also LED60.4 (DO), LED61.2 (DI); no longer LED60.1 (DO), LED61.4 (DI)
- net ROW8: now also LED70.4 (DO), LED71.2 (DI); no longer LED70.1 (DO), LED71.4 (DI)
- net ROW9: now also LED80.4 (DO), LED81.2 (DI); no longer LED80.1 (DO), LED81.4 (DI)
- net at LED42.4 (DO): now also LED43.2 (DI); no longer LED41.1 (DO)
- net at LED38.4 (DO): now also LED39.2 (DI); no longer LED37.1 (DO)
- new net: LED206.4 (DO), LED207.2 (DI)
- new net: LED207.4 (DO), LED208.2 (DI)
- new net: LED537.4 (DO), LED538.2 (DI)
- new net: LED538.4 (DO), LED539.2 (DI)
- new net: LED275.4 (DO), LED276.2 (DI)
- new net: LED276.4 (DO), LED277.2 (DI)
- new net: LED371.4 (DO), LED372.2 (DI)
- new net: LED372.4 (DO), LED373.2 (DI)
- new net: LED281.4 (DO), LED282.2 (DI)
- new net: LED147.4 (DO), LED148.2 (DI)
- new net: LED148.4 (DO), LED149.2 (DI)
- new net: LED318.4 (DO), LED319.2 (DI)
- new net: LED319.4 (DO), LED320.2 (DI)
- new net: LED249.4 (DO), LED250.2 (DI)
- new net: LED114.4 (DO), LED115.2 (DI)
- new net: LED115.4 (DO), LED116.2 (DI)
- new net: LED268.4 (DO), LED269.2 (DI)
- new net: LED269.4 (DO), LED270.2 (DI)
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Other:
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
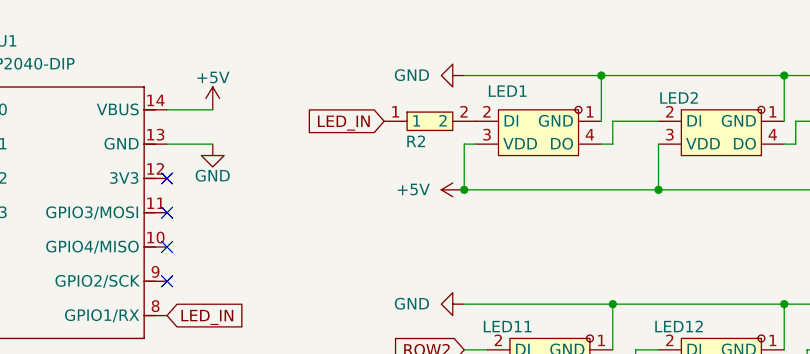
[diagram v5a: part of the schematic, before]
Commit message: Fixed schematic errors
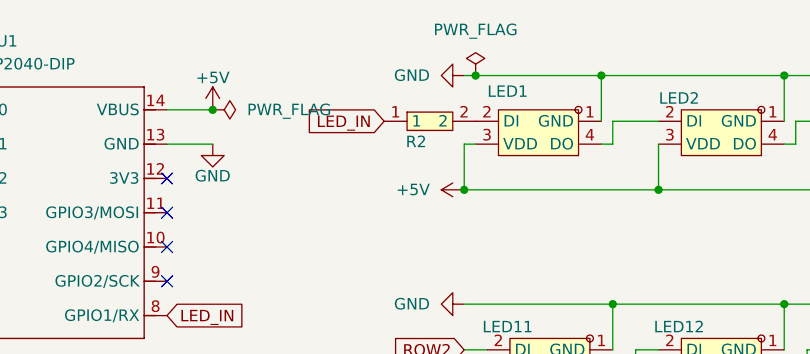
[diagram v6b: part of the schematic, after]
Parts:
- LED1, LED10, LED100, LED101, LED102, LED103, LED104, LED105, LED106, LED107, LED108, LED109, LED11, LED110, LED111, LED112, LED113, LED114, LED115, LED116, LED117, LED118, LED119, LED12, LED120, LED121, LED122, LED123, LED124, LED125, LED126, LED127, LED128, LED129, LED13, LED130, LED131, LED132, LED133, LED134, LED135, LED136, LED137, LED138, LED139, LED14, LED140, LED141, LED142, LED143, LED144, LED145, LED146, LED147, LED148, LED149, LED15, LED150, LED151, LED152, LED153, LED154, LED155, LED156, LED157, LED158, LED159, LED16, LED160, LED161, LED162, LED163, LED164, LED165, LED166, LED167, LED168, LED169, LED17, LED170, LED171, LED172, LED173, LED174, LED175, LED176, LED177, LED178, LED179, LED18, LED180, LED181, LED182, LED183, LED184, LED185, LED186, LED187, LED188, LED189, LED19, LED190, LED191, LED192, LED193, LED194, LED195, LED196, LED197, LED198, LED199, LED2, LED20, LED200, LED201, LED202, LED203, LED204, LED205, LED206, LED207, LED208, LED209, LED21, LED210, LED211, LED212, LED213, LED214, LED215, LED216, LED217, LED218, LED219, LED22, LED220, LED221, LED222, LED223, LED224, LED225, LED226, LED227, LED228, LED229, LED23, LED230, LED231, LED232, LED233, LED234, LED235, LED236, LED237, LED238, LED239, LED24, LED240, LED241, LED242, LED243, LED244, LED245, LED246, LED247, LED248, LED249, LED25, LED250, LED251, LED252, LED253, LED254, LED255, LED256, LED257, LED258, LED259, LED26, LED260, LED261, LED262, LED263, LED264, LED265, LED266, LED267, LED268, LED269, LED27, LED270, LED271, LED272, LED273, LED274, LED275, LED276, LED277, LED278, LED279, LED28, LED280, LED281, LED282, LED283, LED284, LED285, LED286, LED287, LED288, LED289, LED29, LED290, LED291, LED292, LED293, LED294, LED295, LED296, LED297, LED298, LED299, LED3, LED30, LED300, LED301, LED302, LED303, LED304, LED305, LED306, LED307, LED308, LED309, LED31, LED310, LED311, LED312, LED313, LED314, LED315, LED316, LED317, LED318, LED319, LED32, LED320, LED321, LED322, LED323, LED324, LED325, LED326, LED327, LED328, LED329, LED33, LED330, LED331, LED332, LED333, LED334, LED335, LED336, LED337, LED338, LED339, LED34, LED340, LED341, LED342, LED343, LED344, LED345, LED346, LED347, LED348, LED349, LED35, LED350, LED351, LED352, LED353, LED354, LED355, LED356, LED357, LED358, LED359, LED36, LED360, LED361, LED362, LED363, LED364, LED365, LED366, LED367, LED368, LED369, LED37, LED370, LED371, LED372, LED373, LED374, LED375, LED376, LED377, LED378, LED379, LED38, LED380, LED381, LED382, LED383, LED384, LED385, LED386, LED387, LED388, LED389, LED39, LED390, LED391, LED392, LED393, LED394, LED395, LED396, LED397, LED398, LED399, LED4, LED40, LED400, LED401, LED402, LED403, LED404, LED405, LED406, LED407, LED408, LED409, LED41, LED410, LED411, LED412, LED413, LED414, LED415, LED416, LED417, LED418, LED419, LED42, LED420, LED421, LED422, LED423, LED424, LED425, LED426, LED427, LED428, LED429, LED43, LED430, LED431, LED432, LED433, LED434, LED435, LED436, LED437, LED438, LED439, LED44, LED440, LED441, LED442, LED443, LED444, LED445, LED446, LED447, LED448, LED449, LED45, LED450, LED451, LED452, LED453, LED454, LED455, LED456, LED457, LED458, LED459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: footprint JLCPCB-C5349954:LED-SMD_4P-L1.6-W1.5_XL-1615RGBC-WS2812B-1 -> C5349954:LED-SMD_4P-L1.6-W1.5_XL-1615RGBC-WS2812B-1
- R1, R2, R3, R4, R5, R6: footprint Resistor_SMD:R_1206_3216Metric -> C17888:R1206

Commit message: submitted to JLCPCB 2025-Nov-30
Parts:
- LED1, LED10, LED100, LED101, LED102, LED103, LED104, LED105, LED106, LED107, LED108, LED109, LED11, LED110, LED111, LED112, LED113, LED114, LED115, LED116, LED117, LED118, LED119, LED12, LED120, LED121, LED122, LED123, LED124, LED125, LED126, LED127, LED128, LED129, LED13, LED130, LED131, LED132, LED133, LED134, LED135, LED136, LED137, LED138, LED139, LED14, LED140, LED141, LED142, LED143, LED144, LED145, LED146, LED147, LED148, LED149, LED15, LED150, LED151, LED152, LED153, LED154, LED155, LED156, LED157, LED158, LED159, LED16, LED160, LED161, LED162, LED163, LED164, LED165, LED166, LED167, LED168, LED169, LED17, LED170, LED171, LED172, LED173, LED174, LED175, LED176, LED177, LED178, LED179, LED18, LED180, LED181, LED182, LED183, LED184, LED185, LED186, LED187, LED188, LED189, LED19, LED190, LED191, LED192, LED193, LED194, LED195, LED196, LED197, LED198, LED199, LED2, LED20, LED200, LED201, LED202, LED203, LED204, LED205, LED206, LED207, LED208, LED209, LED21, LED210, LED211, LED212, LED213, LED214, LED215, LED216, LED217, LED218, LED219, LED22, LED220, LED221, LED222, LED223, LED224, LED225, LED226, LED227, LED228, LED229, LED23, LED230, LED231, LED232, LED233, LED234, LED235, LED236, LED237, LED238, LED239, LED24, LED240, LED241, LED242, LED243, LED244, LED245, LED246, LED247, LED248, LED249, LED25, LED250, LED251, LED252, LED253, LED254, LED255, LED256, LED257, LED258, LED259, LED26, LED260, LED261, LED262, LED263, LED264, LED265, LED266, LED267, LED268, LED269, LED27, LED270, LED271, LED272, LED273, LED274, LED275, LED276, LED277, LED278, LED279, LED28, LED280, LED281, LED282, LED283, LED284, LED285, LED286, LED287, LED288, LED289, LED29, LED290, LED291, LED292, LED293, LED294, LED295, LED296, LED297, LED298, LED299, LED3, LED30, LED300, LED301, LED302, LED303, LED304, LED305, LED306, LED307, LED308, LED309, LED31, LED310, LED311, LED312, LED313, LED314, LED315, LED316, LED317, LED318, LED319, LED32, LED320, LED321, LED322, LED323, LED324, LED325, LED326, LED327, LED328, LED329, LED33, LED330, LED331, LED332, LED333, LED334, LED335, LED336, LED337, LED338, LED339, LED34, LED340, LED341, LED342, LED343, LED344, LED345, LED346, LED347, LED348, LED349, LED35, LED350, LED351, LED352, LED353, LED354, LED355, LED356, LED357, LED358, LED359, LED36, LED360, LED361, LED362, LED363, LED364, LED365, LED366, LED367, LED368, LED369, LED37, LED370, LED371, LED372, LED373, LED374, LED375, LED376, LED377, LED378, LED379, LED38, LED380, LED381, LED382, LED383, LED384, LED385, LED386, LED387, LED388, LED389, LED39, LED390, LED391, LED392, LED393, LED394, LED395, LED396, LED397, LED398, LED399, LED4, LED40, LED400, LED401, LED402, LED403, LED404, LED405, LED406, LED407, LED408, LED409, LED41, LED410, LED411, LED412, LED413, LED414, LED415, LED416, LED417, LED418, LED419, LED42, LED420, LED421, LED422, LED423, LED424, LED425, LED426, LED427, LED428, LED429, LED43, LED430, LED431, LED432, LED433, LED434, LED435, LED436, LED437, LED438, LED439, LED44, LED440, LED441, LED442, LED443, LED444, LED445, LED446, LED447, LED448, LED449, LED45, LED450, LED451, LED452, LED453, LED454, LED455, LED456, LED457, LED458, LED459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: footprint C5349954:LED-SMD_4P-L1.6-W1.5_XL-1615RGBC-WS2812B-1 -> JLCPCB-C5349954:LED-SMD_4P-L1.6-W1.5_XL-1615RGBC-WS2812B-1
- R1, R2, R3, R4, R5, R6: footprint C17888:R1206 -> Resistor_SMD:R_1206_3216Metric
- U1: now not fitted
